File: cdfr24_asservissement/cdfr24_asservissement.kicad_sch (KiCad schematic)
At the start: 60 parts, among them J1 Connecteur batterie, J11 Conn_01x02, J12 Conn_01x02, J13 Connecteur Odométrie, J14 Conn_ST_STDC14, J15 Conn_01x08_Pin, J2 Conn_01x03, J3 Conn_01x05, J3 Connecteur Programmation, J5 Conn_01x03, J5 Conn_01x08_Pin, J6 Connecteur Odométrie, J7 Conn_01x03, Q1 Q_NMOS_GDS, SW1 SW_DIP_x02, U1 STM32F401RCTx, U2 TVN 5-2411WI, U4 LD1117S33TR_SOT223

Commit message: Place components
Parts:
- added C13: 10uF, Capacitor_SMD:C_0805_2012Metric_Pad1.18x1.45mm_HandSolder, symbol Device:C
- added C8: 100nF, Capacitor_SMD:C_0805_2012Metric_Pad1.18x1.45mm_HandSolder, symbol Device:C
- C1: footprint (none) -> Capacitor_SMD:C_0805_2012Metric_Pad1.18x1.45mm_HandSolder
- C2: renamed from C5; footprint (none) -> Capacitor_SMD:C_0805_2012Metric_Pad1.18x1.45mm_HandSolder
- renumbered C15 to C16, C2 to C3, C3 to C4, C4 to C5, C14 to C6, C13 to C7, D7 to D2, D1 to D3, D3 to D4, D4 to D5, J15 to J4, J14 to J5, J3 to J7, J5 to J9, R7 to R10, R4 to R3, R2 to R4, R5 to R6, R3 to R7, U4 to U1, U1 to U3
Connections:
- net +3.3V: now also C13.1, C8.1
- net GND: now also C13.2, C8.2
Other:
- note added: "Bulk capacitor"

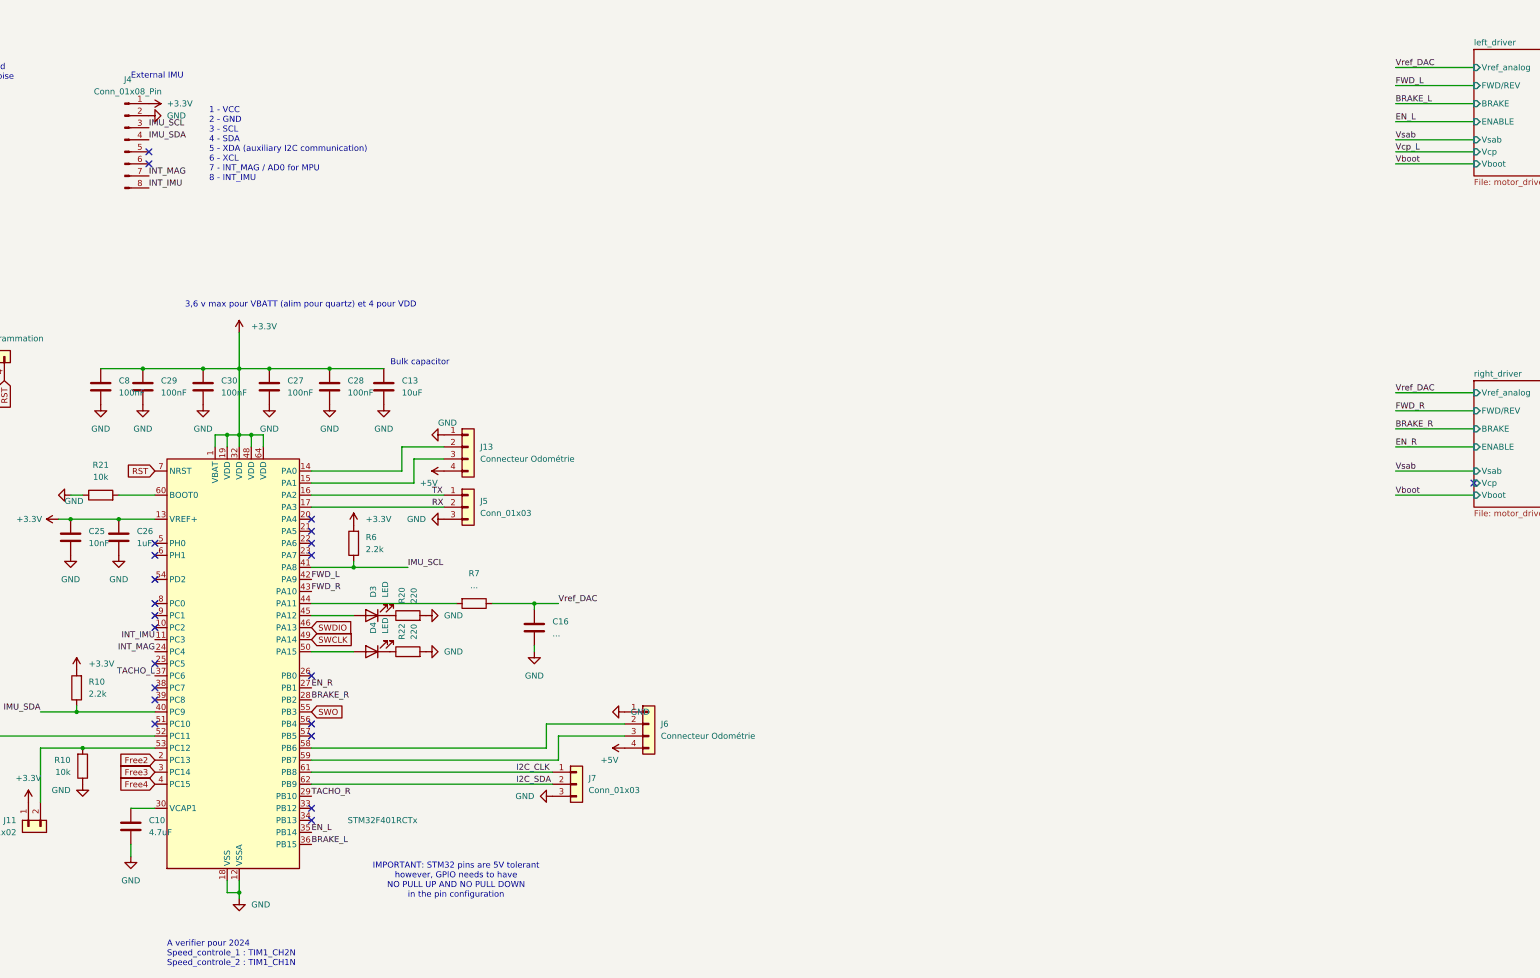
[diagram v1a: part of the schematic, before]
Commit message: Improve placement
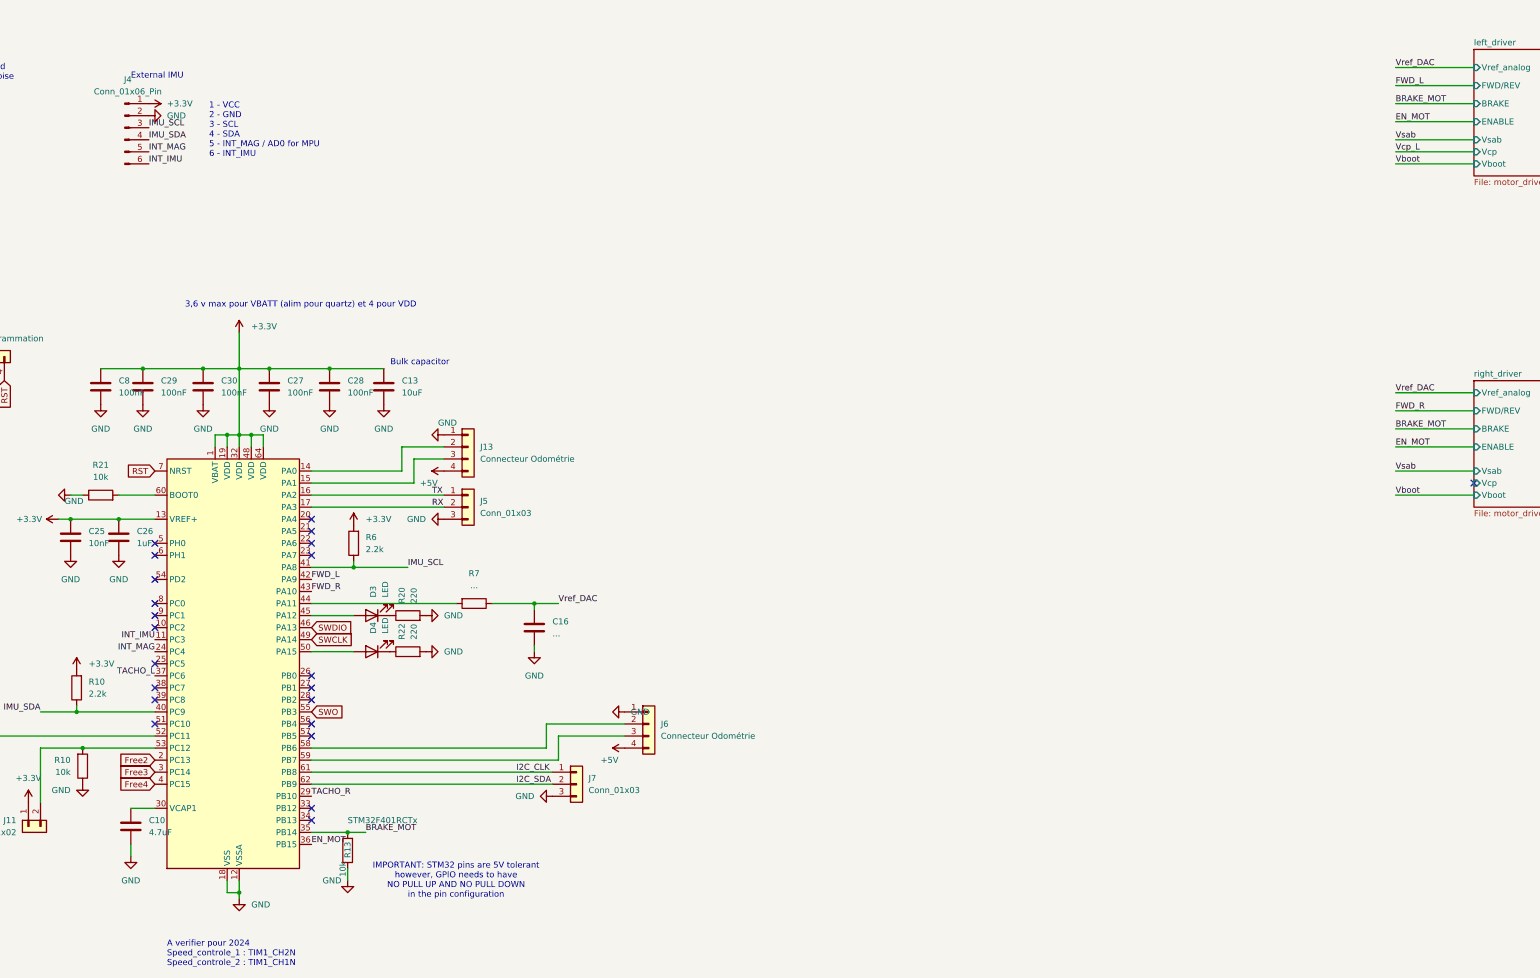
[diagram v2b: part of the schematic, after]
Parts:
- removed J4: Conn_01x08_Pin, Connector_PinHeader_2.54mm:PinHeader_1x08_P2.54mm_Vertical, symbol Connector:Conn_01x08_Pin
- added J4: Conn_01x06_Pin, Connector_PinHeader_2.54mm:PinHeader_1x06_P2.54mm_Vertical, symbol Connector:Conn_01x06_Pin
- added R13: 10k, Resistor_SMD:R_0805_2012Metric_Pad1.20x1.40mm_HandSolder, symbol Device:R
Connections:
- net +3.3V: now also J4.1 (Pin_1)
- net GND: now also J4.2 (Pin_2), R13.1
- net IMU_SCL: now also J4.3 (Pin_3)
- net IMU_SDA: now also J4.4 (Pin_4)
- net INT_IMU: now also J4.6 (Pin_6)
- net INT_MAG: now also J4.5 (Pin_5)
- net BRAKE_L renamed EN_MOT
- net BRAKE_R: no longer names the net of U3.28 (PB2)
- net EN_L renamed BRAKE_MOT
- net BRAKE_MOT: now also R13.2
- net EN_R: no longer names the net of U3.27 (PB1)
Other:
- note added: "1 - VCC 2 - GND 3 - SCL 4 - SDA 5 - INT_MAG / AD0 for MPU 6 - INT_IMU"
- note removed: "1 - VCC 2 - GND 3 - SCL 4 - SDA 5 - XDA (auxiliary I2C communication) 6 - XCL 7 - INT_MAG / AD0 for MPU 8 - INT_IMU"

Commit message: Start routing
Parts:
- removed NT1: NetTie_2, NetTie:NetTie-2_SMD_Pad2.0mm, symbol Device:NetTie_2
- added NT2: NetTie_2, NetTie:NetTie-2_SMD_Pad0.5mm, symbol Device:NetTie_2
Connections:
- net GND: now also NT2.2
- net GNDPWR: now also NT2.1
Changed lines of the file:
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@@
+	)
+	(symbol
+		(lib_id "Device:NetTie_2")
+		(at 139.7 135.89 0)
+		(unit 1)
+		(exclude_from_sim no)
+		(in_bom no)
+		(on_board yes)
+		(dnp no)
+		(fields_autoplaced yes)
+		(property "Reference" "NT2"
+			(at 139.7 130.81 0)
+			(effects
+				(font
+					(size 1.27 1.27)
+				)
+			)
+		)
+		(property "Value" "NetTie_2"
+			(at 139.7 133.35 0)
+			(effects
+				(font
+					(size 1.27 1.27)
+				)
+			)
+		)
+		(property "Footprint" "NetTie:NetTie-2_SMD_Pad0.5mm"
+			(at 139.7 135.89 0)
+			(effects
+				(font
+					(size 1.27 1.27)
+				)
+				(hide yes)
+			)
+		)
+		(property "Datasheet" "~"
+			(at 139.7 135.89 0)
+			(effects
+				(font
+					(size 1.27 1.27)
+				)
+				(hide yes)
+			)
+		)
+		(property "Description" "Net tie, 2 pins"
+			(at 139.7 135.89 0)
+			(effects
+				(font
+					(size 1.27 1.27)
+				)
+				(hide yes)
+			)
+		)
+		(pin "2"
+		)
+		(pin "1"
+		)
+		(instances
+			(project ""
+				(path "/c6b82269-16f5-49e6-8b51-4d12a40a3077"
+					(reference "NT2")
+					(unit 1)
+				)
+			)
+		)
 	)
 	(symbol
@@
 					(unit 1)
 				)
-			)
-		)
-	)
-	(symbol
-		(lib_id "Device:NetTie_2")
-		(at 139.7 135.89 0)
-		(unit 1)
-		(exclude_from_sim yes)
-		(in_bom no)
-		(on_board yes)
-		(dnp no)
-		(fields_autoplaced yes)
-		(property "Reference" "NT1"
-			(at 139.7 130.81 0)
-			(effects
-				(font
-					(size 1.27 1.27)
-				)
-			)
-		)
-		(property "Value" "NetTie_2"
-			(at 139.7 133.35 0)
-			(effects
-				(font
-					(size 1.27 1.27)
-				)
-			)
-		)
-		(property "Footprint" "NetTie:NetTie-2_SMD_Pad2.0mm"
-			(at 139.7 135.89 0)
-			(effects
-				(font
-					(size 1.27 1.27)
-				)
-				(hide yes)
-			)
-		)
-		(property "Datasheet" "~"
-			(at 139.7 135.89 0)
-			(effects
-				(font
-					(size 1.27 1.27)
-				)
-				(hide yes)
-			)
-		)
-		(property "Description" "Net tie, 2 pins"
-			(at 139.7 135.89 0)
-			(effects
-				(font
-					(size 1.27 1.27)
-				)
-				(hide yes)
-			)
-		)
-		(pin "2"
-		)
-		(pin "1"
-		)
-		(instances
-			(project ""
-				(path "/c6b82269-16f5-49e6-8b51-4d12a40a3077"
-					(reference "NT1")
-					(unit 1)
-				)

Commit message: Finish routing
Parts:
- removed J9: Conn_01x08_Pin, Connector_PinHeader_2.54mm:PinHeader_1x08_P2.54mm_Vertical, symbol Connector:Conn_01x08_Pin
- added TP1, TP2, TP3, TP4, TP5, TP6, TP7, TP8: TestPoint, TestPoint:TestPoint_Keystone_5015_Micro-Minature, symbol Connector:TestPoint
- renumbered NT2 to NT1
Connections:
- net +3.3V: now also TP4.1
- net +5V: now also TP7.1
- net +BATT: now also TP5.1
- net FWD_L: now also U3.43 (PA10), TP1.1; no longer U3.42 (PA9)
- net FWD_R: now also U3.42 (PA9), TP2.1; no longer U3.43 (PA10)
- net GND: now also TP8.1
- net GNDPWR: now also TP6.1
- net INT_IMU: now also U3.23 (PA7); no longer U3.11 (PC3)
- net Vref_DAC: now also TP3.1
- net at U3.56 (PB4): now also SW1.2
- net at U3.57 (PB5): now also SW1.1
- net Free2: no longer names the net of U3.2 (PC13)
- net Free3: no longer names the net of U3.3 (PC14)
- net Free4: no longer names the net of U3.4 (PC15)
- no-connect marks 36 -> 30
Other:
- moved on the sheet: SW1

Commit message: Add silkscreen and logo
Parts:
- renumbered TP4 to TP1, TP5 to TP2, TP6 to TP3, TP7 to TP4, TP8 to TP5, TP1 to TP6, TP3 to TP7, TP2 to TP8
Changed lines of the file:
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@@
 			(project "cdfr24_asservissement"
 				(path "/c6b82269-16f5-49e6-8b51-4d12a40a3077"
-					(reference "J13")
+					(reference "J12")
 					(unit 1)
 				)
@@
 			(project "cdfr24_asservissement"
 				(path "/c6b82269-16f5-49e6-8b51-4d12a40a3077"
-					(reference "J10")
+					(reference "J9")
 					(unit 1)
 				)
@@
 		(dnp no)
 		(fields_autoplaced yes)
-		(property "Reference" "TP7"
+		(property "Reference" "TP4"
 			(at 184.15 50.0379 0)
 			(effects
@@
 			(project "cdfr24_asservissement"
 				(path "/c6b82269-16f5-49e6-8b51-4d12a40a3077"
-					(reference "TP7")
+					(reference "TP4")
 					(unit 1)
 				)
@@
 			(project "cdfr24_asservissement"
 				(path "/c6b82269-16f5-49e6-8b51-4d12a40a3077"
-					(reference "J12")
+					(reference "J11")
 					(unit 1)
 				)
@@
 		(dnp no)
 		(fields_autoplaced yes)
-		(property "Reference" "TP8"
+		(property "Reference" "TP5"
 			(at 229.87 57.6579 0)
 			(effects
@@
 			(project "cdfr24_asservissement"
 				(path "/c6b82269-16f5-49e6-8b51-4d12a40a3077"
-					(reference "TP8")
+					(reference "TP5")
 					(unit 1)
 				)
@@
 		(dnp no)
 		(fields_autoplaced yes)
-		(property "Reference" "TP6"
+		(property "Reference" "TP3"
 			(at 156.21 42.4179 0)
 			(effects
@@
 			(project "cdfr24_asservissement"
 				(path "/c6b82269-16f5-49e6-8b51-4d12a40a3077"
-					(reference "TP6")
+					(reference "TP3")
 					(unit 1)
 				)
@@
 			(project "cdfr24_asservissement"
 				(path "/c6b82269-16f5-49e6-8b51-4d12a40a3077"
-					(reference "J14")
+					(reference "J13")
 					(unit 1)
 				)
@@
 		(dnp no)
 		(fields_autoplaced yes)
-		(property "Reference" "TP1"
+		(property "Reference" "TP6"
 			(at 459.74 123.6979 0)
 			(effects
@@
 			(project "cdfr24_asservissement"
 				(path "/c6b82269-16f5-49e6-8b51-4d12a40a3077"
-					(reference "TP1")
+					(reference "TP6")
 					(unit 1)
 				)
@@
 		(dnp no)
 		(fields_autoplaced yes)
-		(property "Reference" "TP2"
+		(property "Reference" "TP8"
 			(at 459.74 192.2779 0)
 			(effects
@@
 			(project ""
 				(path "/c6b82269-16f5-49e6-8b51-4d12a40a3077"
-					(reference "TP2")
+					(reference "TP8")
 					(unit 1)
 				)
@@
 		(dnp no)
 		(fields_autoplaced yes)
-		(property "Reference" "TP5"
+		(property "Reference" "TP2"
 			(at 39.37 42.4179 0)
 			(effects
@@
 			(project "cdfr24_asservissement"
 				(path "/c6b82269-16f5-49e6-8b51-4d12a40a3077"
-					(reference "TP5")
+					(reference "TP2")
 					(unit 1)
 				)
@@
 			(project "cdfr24_asservissement"
 				(path "/c6b82269-16f5-49e6-8b51-4d12a40a3077"
-					(reference "J11")
+					(reference "J10")
 					(unit 1)
 				)
@@
 		(dnp no)
 		(fields_autoplaced yes)
-		(property "Reference" "TP4"
+		(property "Reference" "TP1"
 			(at 270.51 34.7979 0)
 			(effects
@@
 			(project "cdfr24_asservissement"
 				(path "/c6b82269-16f5-49e6-8b51-4d12a40a3077"
-					(reference "TP4")
+					(reference "TP1")
 					(unit 1)
 				)
@@
 			(project "cdfr24_asservissement"
 				(path "/c6b82269-16f5-49e6-8b51-4d12a40a3077"
-					(reference "J15")
+					(reference "J14")
 					(unit 1)
 				)
@@
 		(dnp no)
 		(fields_autoplaced yes)
-		(property "Reference" "TP3"
+		(property "Reference" "TP7"
 			(at 462.28 188.4679 0)
 			(effects
@@
 			(project "cdfr24_asservissement"
 				(path "/c6b82269-16f5-49e6-8b51-4d12a40a3077"
-					(reference "TP3")
+					(reference "TP7")
 					(unit 1)
 				)

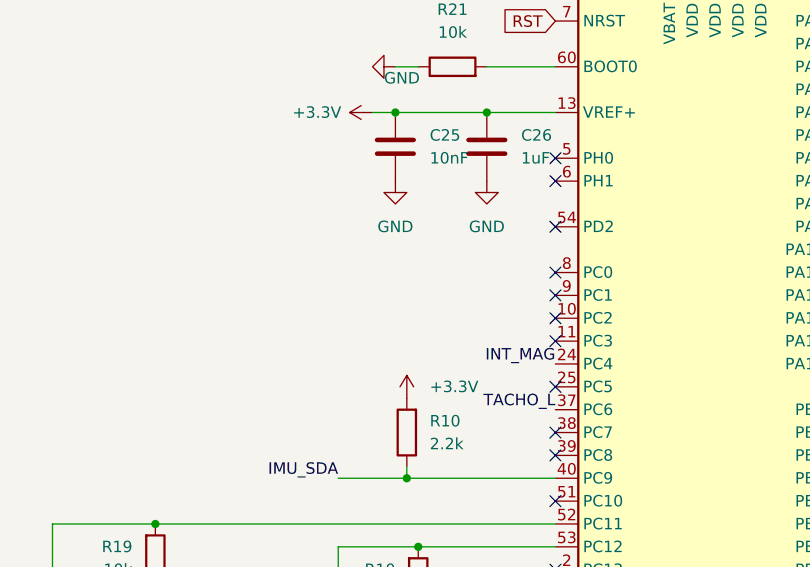
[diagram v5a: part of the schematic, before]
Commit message: Add text on PCB
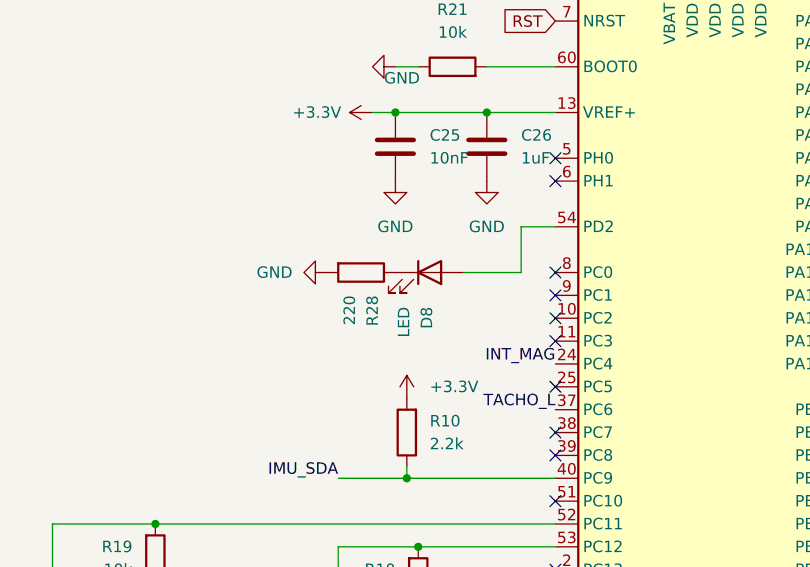
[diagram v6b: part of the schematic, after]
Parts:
- added D8: LED, LED_SMD:LED_0805_2012Metric_Pad1.15x1.40mm_HandSolder, symbol Device:LED
- added R28: 220, Resistor_SMD:R_0805_2012Metric_Pad1.20x1.40mm_HandSolder, symbol Device:R
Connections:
- net GND: now also R28.2
- net at U3.54 (PD2): now also D8.2 (A)
- new net: D8.1 (K), R28.1
- no-connect marks 30 -> 29
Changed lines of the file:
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@@
 	)
 	(no_connect
-		(at 185.42 232.41)
-	)
-	(no_connect
 		(at 218.44 280.67)
 	)
@@
 	(wire
 		(pts
+			(xy 181.61 232.41) (xy 181.61 237.49)
+		)
+		(stroke
+			(width 0)
+			(type default)
+		)
+	)
+	(wire
+		(pts
 			(xy 411.48 74.93) (xy 415.29 74.93)
 		)
@@
 	(wire
 		(pts
+			(xy 181.61 237.49) (xy 175.26 237.49)
+		)
+		(stroke
+			(width 0)
+			(type default)
+		)
+	)
+	(wire
+		(pts
 			(xy 208.28 201.93) (xy 205.74 201.93)
 		)
@@
 	(wire
 		(pts
+			(xy 185.42 232.41) (xy 181.61 232.41)
+		)
+		(stroke
+			(width 0)
+			(type default)
+		)
+	)
+	(wire
+		(pts
 			(xy 250.19 39.37) (xy 262.89 39.37)
 		)
@@
 	)
 	(symbol
+		(lib_id "Device:LED")
+		(at 171.45 237.49 0)
+		(unit 1)
+		(exclude_from_sim yes)
+		(in_bom yes)
+		(on_board yes)
+		(dnp no)
+		(fields_autoplaced yes)
+		(property "Reference" "D8"
+			(at 171.1326 241.3 90)
+			(effects
+				(font
+					(size 1.27 1.27)
+				)
+				(justify right)
+			)
+		)
+		(property "Value" "LED"
+			(at 168.5926 241.3 90)
+			(effects
+				(font
+					(size 1.27 1.27)
+				)
+				(justify right)
+			)
+		)
+		(property "Footprint" "LED_SMD:LED_0805_2012Metric_Pad1.15x1.40mm_HandSolder"
+			(at 171.45 237.49 0)
+			(effects
+				(font
+					(size 1.27 1.27)
+				)
+				(hide yes)
+			)
+		)
+		(property "Datasheet" "~"
+			(at 171.45 237.49 0)
+			(effects
+				(font
+					(size 1.27 1.27)
+				)
+				(hide yes)
+			)
+		)
+		(property "Description" ""
+			(at 171.45 237.49 0)
+			(effects
+				(font
+					(size 1.27 1.27)
+				)
+				(hide yes)
+			)
+		)
+		(pin "1"
+		)
+		(pin "2"
+		)
+		(instances
+			(project "cdfr24_asservissement"
+				(path "/c6b82269-16f5-49e6-8b51-4d12a40a3077"
+					(reference "D8")
+					(unit 1)
+				)
+			)
+		)
+	)
+	(symbol
 		(lib_id "TVN-5-2411WI:TVN_5-2411WI")
 		(at 71.12 46.99 0)
@@
 	)
 	(symbol
+		(lib_id "power:GND")
+		(at 160.02 237.49 270)
+		(unit 1)
+		(exclude_from_sim no)
+		(in_bom yes)
+		(on_board yes)
+		(dnp no)
+		(fields_autoplaced yes)
+		(property "Reference" "#PWR073"
+			(at 153.67 237.49 0)
+			(effects
+				(font
+					(size 1.27 1.27)
+				)
+				(hide yes)
+			)
+		)
+		(property "Value" "GND"
+			(at 156.21 237.4901 90)
+			(effects
+				(font
+					(size 1.27 1.27)
+				)
+				(justify right)
+			)
+		)
+		(property "Footprint" ""
+			(at 160.02 237.49 0)
+			(effects
+				(font
+					(size 1.27 1.27)
+				)
+				(hide yes)
+			)
+		)
+		(property "Datasheet" ""
+			(at 160.02 237.49 0)
+			(effects
+				(font
+					(size 1.27 1.27)
+				)
+				(hide yes)
+			)
+		)
+		(property "Description" "Power symbol creates a global label with name \"GND\" , ground"
+			(at 160.02 237.49 0)
+			(effects
+				(font
+					(size 1.27 1.27)
+				)
+				(hide yes)
+			)
+		)
+		(pin "1"
+		)
+		(instances
+			(project "cdfr24_asservissement"
+				(path "/c6b82269-16f5-49e6-8b51-4d12a40a3077"
+					(reference "#PWR073")
+					(unit 1)
+				)
+			)
+		)
+	)
+	(symbol
 		(lib_id "Device:C")
 		(at 222.25 191.77 0)
@@
 					(unit 1)
 				)
+			)
+		)
+	)
+	(symbol
+		(lib_id "Device:R")
+		(at 163.83 237.49 270)
+		(unit 1)
+		(exclude_from_sim no)
+		(in_bom yes)
+		(on_board yes)
+		(dnp no)
+		(fields_autoplaced yes)
+		(property "Reference" "R28"
+			(at 165.1001 240.03 0)
+			(effects
+				(font
+					(size 1.27 1.27)
+				)
+				(justify left)
+			)
+		)
+		(property "Value" "220"
+			(at 162.5601 240.03 0)
+			(effects
+				(font
+					(size 1.27 1.27)
+				)
+				(justify left)
+			)
+		)
+		(property "Footprint" "Resistor_SMD:R_0805_2012Metric_Pad1.20x1.40mm_HandSolder"
+			(at 163.83 235.712 90)
+			(effects
+				(font
+					(size 1.27 1.27)
+				)
+				(hide yes)
+			)
+		)
+		(property "Datasheet" "~"
+			(at 163.83 237.49 0)
+			(effects
+				(font
+					(size 1.27 1.27)
+				)
+				(hide yes)
+			)
+		)
+		(property "Description" ""
+			(at 163.83 237.49 0)
+			(effects
+				(font
+					(size 1.27 1.27)
+				)
+				(hide yes)
+			)
+		)
+		(pin "1"
+		)
+		(pin "2"
+		)
+		(instances
+			(project "cdfr24_asservissement"
+				(path "/c6b82269-16f5-49e6-8b51-4d12a40a3077"
+					(reference "R28")
+					(unit 1)
+				)
